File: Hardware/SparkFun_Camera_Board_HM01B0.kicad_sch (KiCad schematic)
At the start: 45 parts, among them J1 Conn_01x09, J2 Conn_01x09, J3 Conn_01x09, J4 HM01B0, Q1 RE1C002UNTCL, Q2 RE1C002UNTCL, Q3 RE1C002UNTCL, Q4 RE1C002UNTCL, U1 HM01B0, U2 RT9080-2.8V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

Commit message: Rename MCLK to XCLK
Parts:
- JP4: value MCLK -> XCLK
- JP6: value MCLK_GND -> XCLK_GND
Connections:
- net CAM_MCLK renamed CAM_XCLK
- net MCLK renamed XCLK
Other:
- note added: "Connect XCLK to only 1 at a time, otherwise undefined behavior or damage may occur"
- note added: "XCLK Generator and Selection"
- note added: "XCLK PTH Pad"
- note removed: "Connect MCLK to only 1 at a time, otherwise undefined behavior or damage may occur"
- note removed: "MCLK Generator and Selection"
- note removed: "MCLK PTH Pad"
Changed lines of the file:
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@@
 		)
 	)
-	(text "Connect MCLK to only 1 at\na time, otherwise undefined\nbehavior or damage may occur"
+	(text "Connect XCLK to only 1 at\na time, otherwise undefined\nbehavior or damage may occur"
 		(exclude_from_sim no)
 		(at 245.11 102.87 0)
@@
 		)
 	)
-	(text "MCLK Generator and Selection"
+	(text "XCLK Generator and Selection"
 		(exclude_from_sim no)
 		(at 215.9 74.93 0)
@@
 		)
 	)
-	(text "MCLK PTH Pad"
+	(text "XCLK PTH Pad"
 		(exclude_from_sim no)
 		(at 233.68 113.03 0)
@@
 		)
 	)
-	(global_label "CAM_MCLK"
+	(global_label "CAM_XCLK"
 		(shape input)
 		(at 63.5 63.5 0)
@@
 		)
 	)
-	(global_label "MCLK"
+	(global_label "XCLK"
 		(shape input)
 		(at 243.84 40.64 0)
@@
 		)
 	)
-	(global_label "MCLK"
+	(global_label "XCLK"
 		(shape input)
 		(at 215.9 40.64 0)
@@
 		)
 	)
-	(global_label "CAM_MCLK"
+	(global_label "CAM_XCLK"
 		(shape input)
 		(at 228.6 91.44 0)
@@
 		)
 	)
-	(global_label "MCLK"
+	(global_label "XCLK"
 		(shape input)
 		(at 223.52 86.36 0)
@@
 			)
 		)
-		(property "Value" "MCLK"
+		(property "Value" "XCLK"
 			(at 217.17 91.44 90)
 			(effects
@@
 			)
 		)
-		(property "Value" "MCLK_GND"
+		(property "Value" "XCLK_GND"
 			(at 228.6 96.52 90)
 			(effects

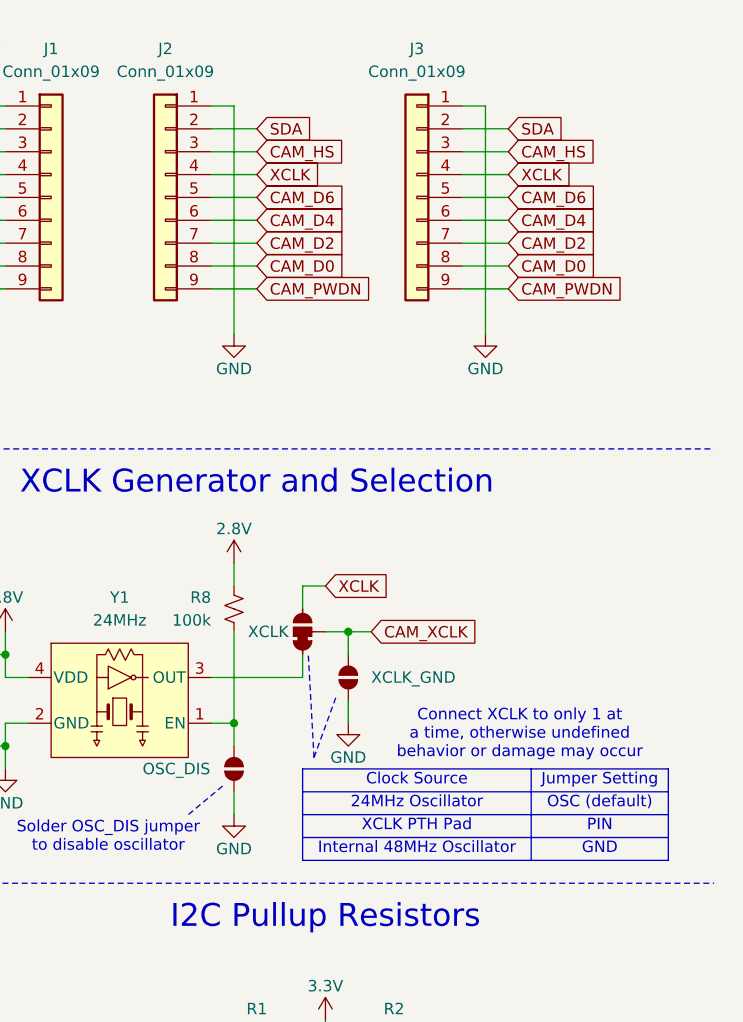
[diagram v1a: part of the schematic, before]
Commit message: Change XCLK jumpers to 3x 2-pad jumpers
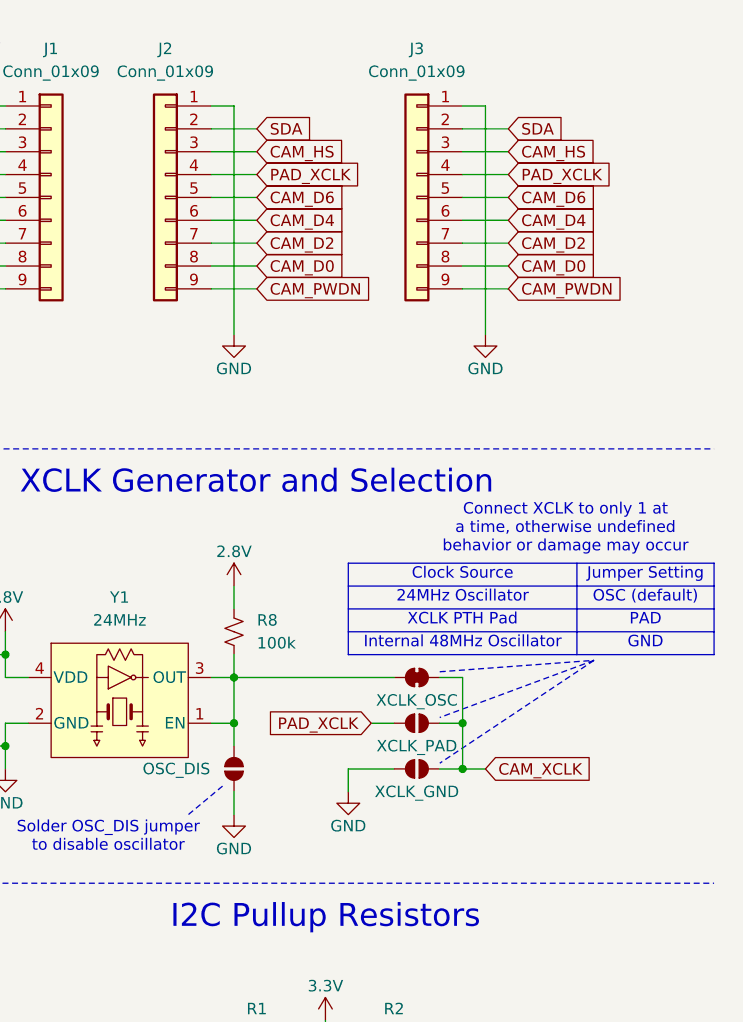
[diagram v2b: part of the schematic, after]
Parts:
- removed JP4: XCLK, SparkFun-Jumper:Jumper_3_NC-1_Trace, symbol SparkFun-Jumper:SolderJumper_3_Bridged12
- added JP2: XCLK_PAD, SparkFun-Jumper:Jumper_2_NO_NoSilk, symbol SparkFun-Jumper:SolderJumper_2_Open_No_Silk
- added JP3: XCLK_OSC, SparkFun-Jumper:Jumper_2_NC_Trace_NoSilk, symbol SparkFun-Jumper:SolderJumper_2_Bridged_No_Silk
- JP6: footprint SparkFun-Jumper:Jumper_2_NO -> SparkFun-Jumper:Jumper_2_NO_NoSilk; symbol SparkFun-Jumper:SolderJumper_2_Open -> SparkFun-Jumper:SolderJumper_2_Open_No_Silk
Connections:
- net CAM_XCLK: now also JP2.2 (B), JP3.2 (B)
- net at Y1.3 (OUT): now also JP5.2 (B), R8.1, Y1.1 (EN), JP3.1 (A)
- net XCLK renamed PAD_XCLK
- net PAD_XCLK: now also JP2.1 (A)
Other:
- note added: "PAD"
- note removed: "PIN"
- moved on the sheet: R8

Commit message: Save schematic....
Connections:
- net at JP5.2 (B), R8.1, Y1.1 (EN): no longer JP3.1 (A), Y1.3 (OUT)
- new net: JP3.1 (A), Y1.3 (OUT)
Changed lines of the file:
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@@
-	)
-	(junction
-		(at 213.36 96.52)
-		(diameter 0)
-		(color 0 0 0 0)
 	)
 	(junction
@@
 	(wire
 		(pts
-			(xy 213.36 96.52) (xy 231.14 96.52)
+			(xy 210.82 96.52) (xy 231.14 96.52)
 		)
 		(stroke
@@
 	(wire
 		(pts
-			(xy 213.36 96.52) (xy 213.36 101.6)
-		)
-		(stroke
-			(width 0)
-			(type default)
-		)
-	)
-	(wire
-		(pts
-			(xy 213.36 93.98) (xy 213.36 96.52)
+			(xy 213.36 93.98) (xy 213.36 101.6)
 		)
 		(stroke
@@
 		)
 		(stroke
-			(width 0)
-			(type default)
-		)
-	)
-	(wire
-		(pts
-			(xy 210.82 96.52) (xy 213.36 96.52)
-		)
-		(stroke
